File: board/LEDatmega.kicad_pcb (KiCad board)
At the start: 2 copper layers, 38.1 x 53.8 mm, 11 parts, among them J1 Conn_01x04, J2 Conn_02x03_Odd_Even, Q1 BC337, U1 ATMEGA8-16PU, U2 TSOP312xx

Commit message: Layouting done
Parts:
- removed C1: 4.7u, Capacitor_THT:CP_Radial_D8.0mm_P3.80mm
- removed D1: SFH409-2, LED_THT:LED_D4.0mm
- removed Q1: BC337, Package_TO_SOT_THT:TO-92_Inline_Wide
- removed R2: 33, Resistor_THT:R_Axial_DIN0207_L6.3mm_D2.5mm_P10.16mm_Horizontal
- removed R3: 100, Resistor_THT:R_Axial_DIN0207_L6.3mm_D2.5mm_P10.16mm_Horizontal
- removed U2: TSOP312xx, OptoDevice:Vishay_CAST-3Pin
- added J3: Conn_01x03, Connector_PinSocket_2.54mm:PinSocket_1x03_P2.54mm_Vertical, F.Cu at (57.1, 65.4)
- added J4: Conn_01x02_Male, Connector_PinSocket_2.54mm:PinSocket_1x02_P2.54mm_Vertical, F.Cu at (55.9, 92.1)
- added J5: Conn_01x02_Male, Connector_PinSocket_2.54mm:PinSocket_1x02_P2.54mm_Vertical, F.Cu at (54.6, 85.7)
- added J6: Conn_01x02_Male, Connector_PinSocket_2.54mm:PinSocket_1x02_P2.54mm_Vertical, F.Cu at (52.1, 92.1)
- J1: value Conn_01x04 -> Conn_01x06_Male; footprint Connector_PinHeader_2.54mm:PinHeader_1x04_P2.54mm_Vertical -> Connector_PinSocket_2.54mm:PinSocket_1x06_P2.54mm_Vertical
- R1: value 1K -> 100k
- moved R4 14.1 mm to (61.6, 65.4)
- moved J1 6.91 mm to (63.5, 58.4), turned to 270 degrees
- moved R1 5.03 mm to (59.1, 92.1)
- moved J2 2.69 mm to (77.9, 89.5)
- moved U1 2.69 mm to (70.7, 49.9)
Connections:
- J1 pad 1: +5V -> GND
- J1 pad 2: Net-(J1-Pad2) -> (no net)
- J1 pad 3: Net-(J1-Pad3) -> (no net)
- J1 pad 4: GND -> Net-(J1-Pad4)
- J2 pad 2: Net-(J2-Pad2) -> (no net)
- R1 pad 1: Net-(Q1-Pad2) -> Net-(J5-Pad1)
- R1 pad 2: MOSI -> GND
- U1 pad 10: Net-(U1-Pad10) -> (no net)
- U1 pad 11: Net-(U1-Pad11) -> (no net)
- U1 pad 12: Net-(U1-Pad12) -> (no net)
- U1 pad 13: Net-(U1-Pad13) -> (no net)
- U1 pad 14: Net-(U1-Pad14) -> (no net)
- U1 pad 15: Net-(U1-Pad15) -> (no net)
- U1 pad 16: Net-(U1-Pad16) -> (no net)
- U1 pad 2: Net-(J1-Pad2) -> Net-(J1-Pad5)
- U1 pad 21: Net-(U1-Pad21) -> (no net)
- U1 pad 23: Net-(U1-Pad23) -> (no net)
- U1 pad 24: Net-(U1-Pad24) -> (no net)
- U1 pad 25: Net-(U1-Pad25) -> (no net)
- U1 pad 26: Net-(U1-Pad26) -> (no net)
- U1 pad 27: Net-(U1-Pad27) -> (no net)
- U1 pad 28: Net-(U1-Pad28) -> (no net)
- U1 pad 3: Net-(J1-Pad3) -> Net-(J1-Pad4)
- U1 pad 4: Net-(U1-Pad4) -> (no net)
- U1 pad 5: Net-(U1-Pad5) -> LED
- U1 pad 6: Net-(U1-Pad6) -> Net-(J5-Pad1)
- U1 pad 9: Net-(U1-Pad9) -> (no net)
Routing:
- net Net-(J5-Pad1): track 0.00 -> 44.2 mm, vias 0 -> 2
- net LED: track 0.00 -> 23.7 mm
- net Net-(U1-Pad9): track 23.2 -> 0.00 mm
- net Net-(J1-Pad5): track 0.00 -> 22.5 mm
- net RESET: track 99.4 -> 77.2 mm
- net Net-(C1-Pad1): track 19.7 -> 0.00 mm
- net GND: track 42.1 -> 60.1 mm, vias 4 -> 2
- net Net-(J1-Pad4): track 0.00 -> 17.8 mm
- net Net-(D1-Pad1): track 9.86 -> 0.00 mm
- net Net-(D1-Pad2): track 9.78 -> 0.00 mm
- net Net-(Q1-Pad2): track 8.71 -> 0.00 mm
- net MOSI: track 40.7 -> 32.8 mm
- net Net-(J1-Pad3): track 7.11 -> 0.00 mm
- net Net-(J1-Pad2): track 7.11 -> 0.00 mm
- net +5V: track 60.9 -> 64.5 mm, vias 0 -> 2
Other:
- board text added: "GND TX RX"
- board text removed: "GND TX RX 5V"

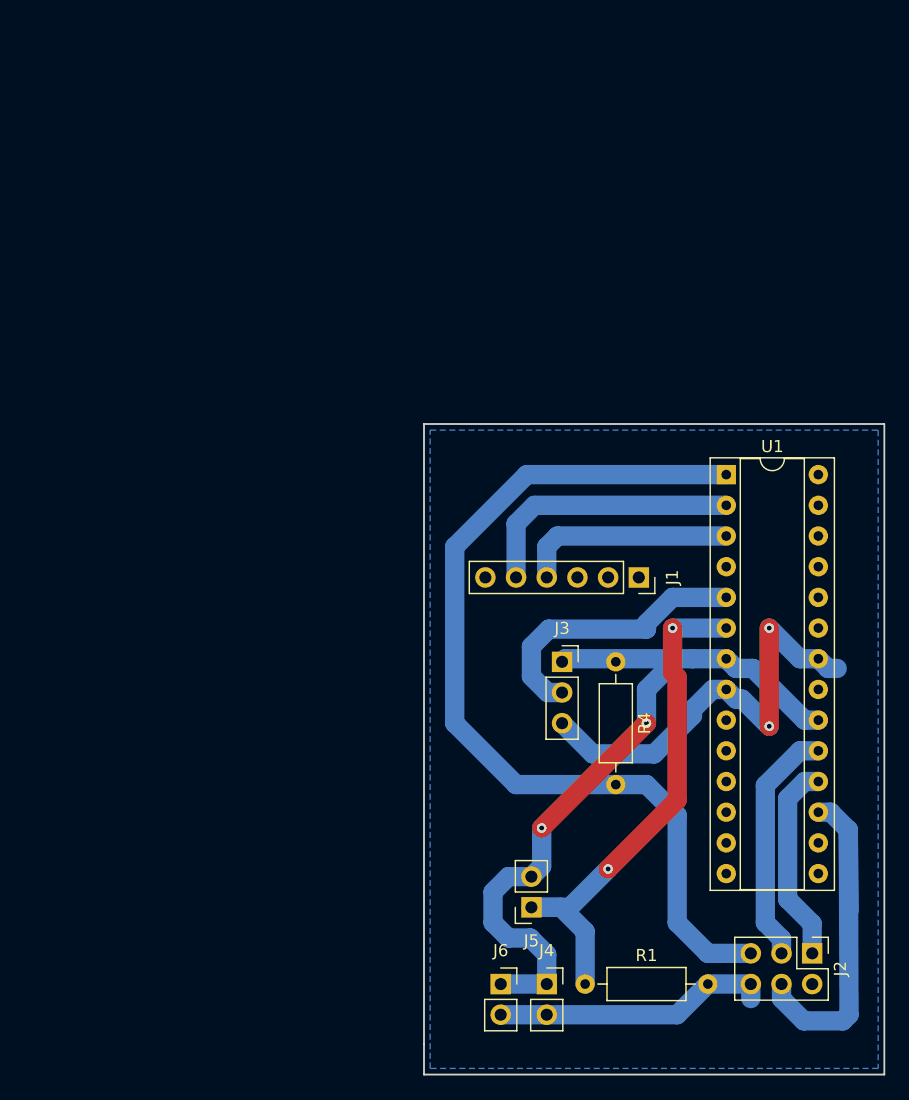
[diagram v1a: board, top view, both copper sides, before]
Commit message: Moved board in the upper left corner
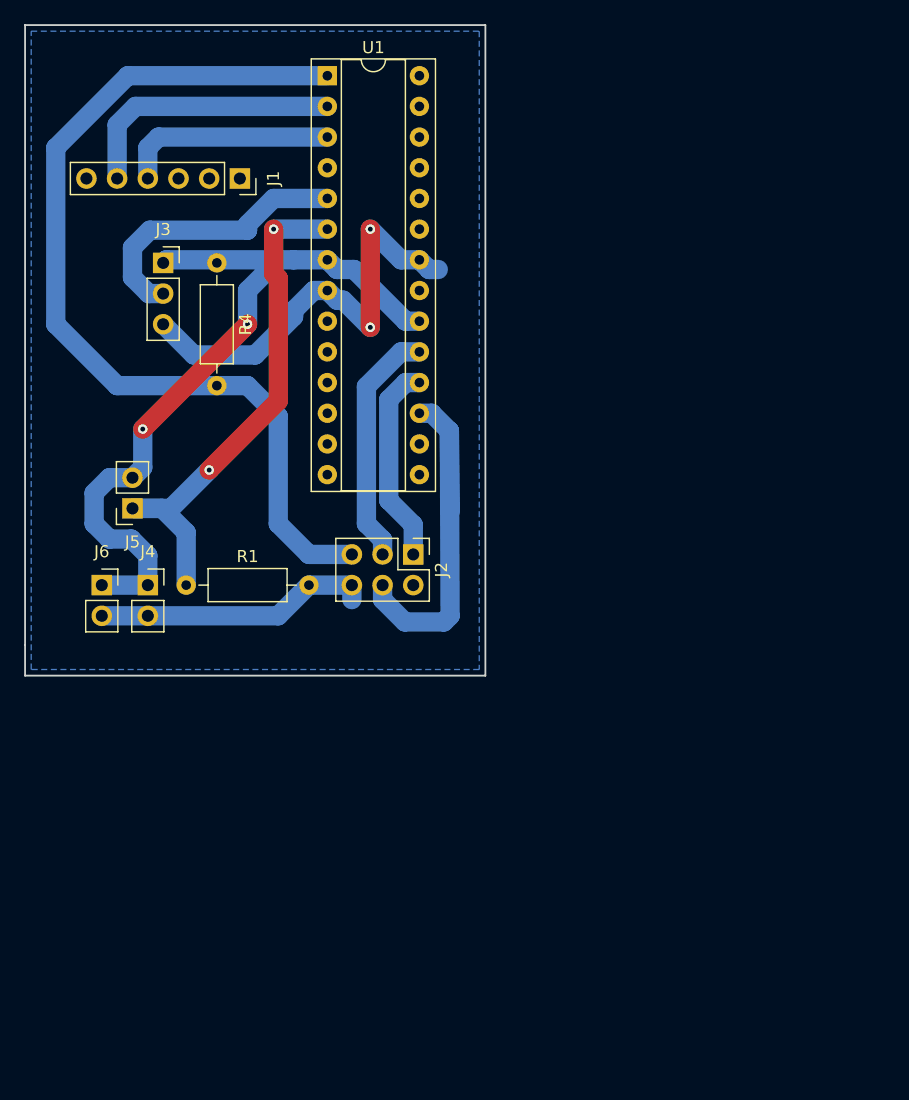
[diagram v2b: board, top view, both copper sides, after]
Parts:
- moved J4 46.7 mm to (22.9, 59.1)
- moved U1 46.7 mm to (37.7, 16.9)
- moved J1 46.7 mm to (30.5, 25.4)
- moved J3 46.7 mm to (24.1, 32.4)
- moved J6 46.7 mm to (19.0, 59.1)
- moved R1 46.7 mm to (26.0, 59.1)
- moved R4 46.7 mm to (28.6, 32.4)
- moved J2 46.7 mm to (44.8, 56.5)
- moved J5 46.7 mm to (21.6, 52.7)

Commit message: Only 3pin connector for Serial interface
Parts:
- J1: value Conn_01x06_Male -> Conn_01x03_Female; footprint Connector_PinSocket_2.54mm:PinSocket_1x06_P2.54mm_Vertical -> Connector_PinHeader_2.54mm:PinHeader_1x03_P2.54mm_Vertical
- moved J1 5.75 mm to (29.8, 19.7), turned to 0 degrees
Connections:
- J1 pad 1: GND -> Net-(J1-Pad1)
- J1 pad 2: (no net) -> Net-(J1-Pad2)
- J1 pad 3: (no net) -> GND
- U1 pad 2: Net-(J1-Pad5) -> Net-(J1-Pad1)
- U1 pad 3: Net-(J1-Pad4) -> Net-(J1-Pad2)
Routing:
- net Net-(J1-Pad5): track 22.5 -> 0.00 mm
- net Net-(J1-Pad4): track 17.8 -> 0.00 mm
- net Net-(J1-Pad2): track 0.00 -> 7.98 mm
- net Net-(J1-Pad1): track 0.00 -> 7.98 mm
- net RESET: track 77.2 -> 74.1 mm
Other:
- board text added: "5V GND"
- board text added: "5V WS2812 GND"
- board text added: "Button"
